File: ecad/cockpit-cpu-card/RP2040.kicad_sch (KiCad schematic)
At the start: 66 parts, among them J6 CONSOLE, J7 USB_B_Micro, J8 GamePort, SW1 USB_PGM, SW2 USB_PGM, U4 IS25LP128F-JBLE, U5 RP2040, Y1 12MHz

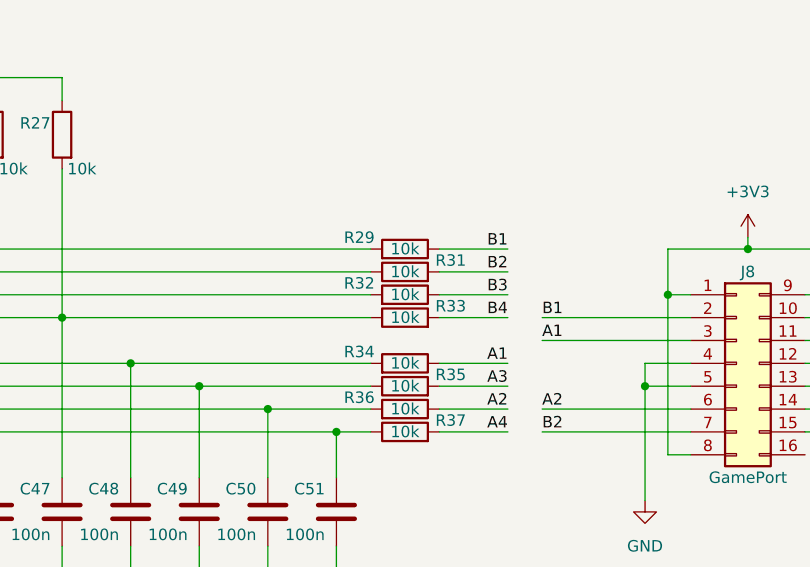
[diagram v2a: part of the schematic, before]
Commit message: Updating resistor values
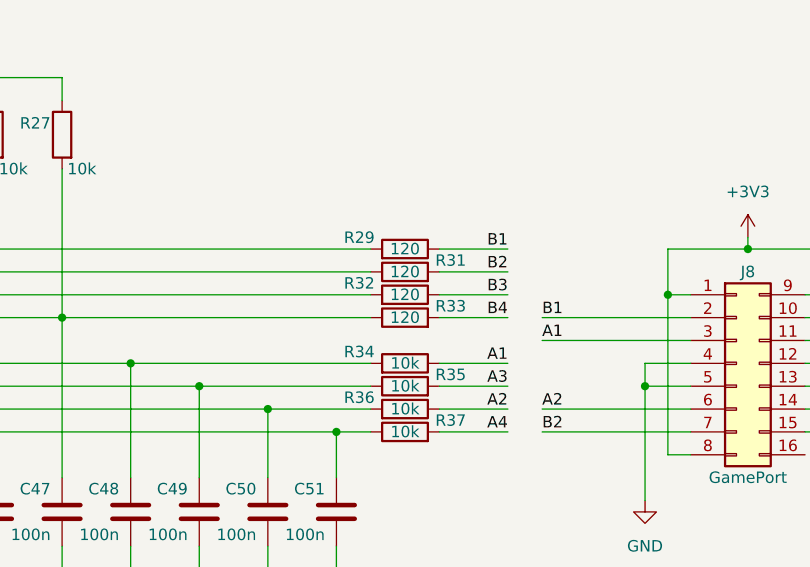
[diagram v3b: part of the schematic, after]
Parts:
- R29, R31, R32: value 10k -> 120; MPN MCMR06X103 JTL -> 1550603SAF1200T5E; ON_DISTRELEC (none) -> 300-56-474; ON_FARNELL 2073356 -> (none)
- R33: value 10k -> 120; MPN MCMR06X103 JTL -> 1550603SAF1200T5E; ON_DISTRELEC (none) -> 300-56-474
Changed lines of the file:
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@@
     (in_bom yes) (on_board yes)
     (property "Reference" "R31" (id 0) (at 218.44 118.11 90))
-    (property "Value" "10k" (id 1) (at 213.36 119.38 90))
+    (property "Value" "120" (id 1) (at 213.36 119.38 90))
     (property "Footprint" "Resistor_SMD:R_0603_1608Metric" (id 2) (at 213.36 121.158 90)
       (effects (font (size 1.27 1.27)) hide)
@@
       (effects (font (size 1.27 1.27)) hide)
     )
-    (property "MPN" "MCMR06X103 JTL" (id 4) (at 213.36 119.38 0)
-      (effects (font (size 1.27 1.27)) hide)
-    )
-    (property "ON_FARNELL" "2073356" (id 5) (at 213.36 119.38 0)
+    (property "MPN" "1550603SAF1200T5E" (id 4) (at 213.36 119.38 0)
+      (effects (font (size 1.27 1.27)) hide)
+    )
+    (property "ON_FARNELL" "" (id 5) (at 213.36 119.38 0)
+      (effects (font (size 1.27 1.27)) hide)
+    )
+    (property "ON_DISTRELEC" "300-56-474" (id 6) (at 213.36 119.38 0)
       (effects (font (size 1.27 1.27)) hide)
     )
@@
     (in_bom yes) (on_board yes)
     (property "Reference" "R29" (id 0) (at 208.28 115.57 90))
-    (property "Value" "10k" (id 1) (at 213.36 116.84 90))
+    (property "Value" "120" (id 1) (at 213.36 116.84 90))
     (property "Footprint" "Resistor_SMD:R_0603_1608Metric" (id 2) (at 213.36 118.618 90)
       (effects (font (size 1.27 1.27)) hide)
@@
       (effects (font (size 1.27 1.27)) hide)
     )
-    (property "MPN" "MCMR06X103 JTL" (id 4) (at 213.36 116.84 0)
-      (effects (font (size 1.27 1.27)) hide)
-    )
-    (property "ON_FARNELL" "2073356" (id 5) (at 213.36 116.84 0)
+    (property "MPN" "1550603SAF1200T5E" (id 4) (at 213.36 116.84 0)
+      (effects (font (size 1.27 1.27)) hide)
+    )
+    (property "ON_FARNELL" "" (id 5) (at 213.36 116.84 0)
+      (effects (font (size 1.27 1.27)) hide)
+    )
+    (property "ON_DISTRELEC" "300-56-474" (id 6) (at 213.36 116.84 0)
       (effects (font (size 1.27 1.27)) hide)
     )
@@
     (in_bom yes) (on_board yes)
     (property "Reference" "R32" (id 0) (at 208.28 120.65 90))
-    (property "Value" "10k" (id 1) (at 213.36 121.92 90))
+    (property "Value" "120" (id 1) (at 213.36 121.92 90))
     (property "Footprint" "Resistor_SMD:R_0603_1608Metric" (id 2) (at 213.36 123.698 90)
       (effects (font (size 1.27 1.27)) hide)
@@
       (effects (font (size 1.27 1.27)) hide)
     )
-    (property "MPN" "MCMR06X103 JTL" (id 4) (at 213.36 121.92 0)
-      (effects (font (size 1.27 1.27)) hide)
-    )
-    (property "ON_FARNELL" "2073356" (id 5) (at 213.36 121.92 0)
+    (property "MPN" "1550603SAF1200T5E" (id 4) (at 213.36 121.92 0)
+      (effects (font (size 1.27 1.27)) hide)
+    )
+    (property "ON_FARNELL" "" (id 5) (at 213.36 121.92 0)
+      (effects (font (size 1.27 1.27)) hide)
+    )
+    (property "ON_DISTRELEC" "300-56-474" (id 6) (at 213.36 121.92 0)
       (effects (font (size 1.27 1.27)) hide)
     )
@@
     (in_bom yes) (on_board yes)
     (property "Reference" "R33" (id 0) (at 218.44 123.19 90))
-    (property "Value" "10k" (id 1) (at 213.36 124.46 90))
+    (property "Value" "120" (id 1) (at 213.36 124.46 90))
     (property "Footprint" "Resistor_SMD:R_0603_1608Metric" (id 2) (at 213.36 126.238 90)
       (effects (font (size 1.27 1.27)) hide)
@@
       (effects (font (size 1.27 1.27)) hide)
     )
-    (property "MPN" "MCMR06X103 JTL" (id 4) (at 213.36 124.46 0)
+    (property "MPN" "1550603SAF1200T5E" (id 4) (at 213.36 124.46 0)
       (effects (font (size 1.27 1.27)) hide)
     )
@@
       (effects (font (size 1.27 1.27)) hide)
     )
+    (property "ON_DISTRELEC" "300-56-474" (id 6) (at 213.36 124.46 0)
+      (effects (font (size 1.27 1.27)) hide)
+    )

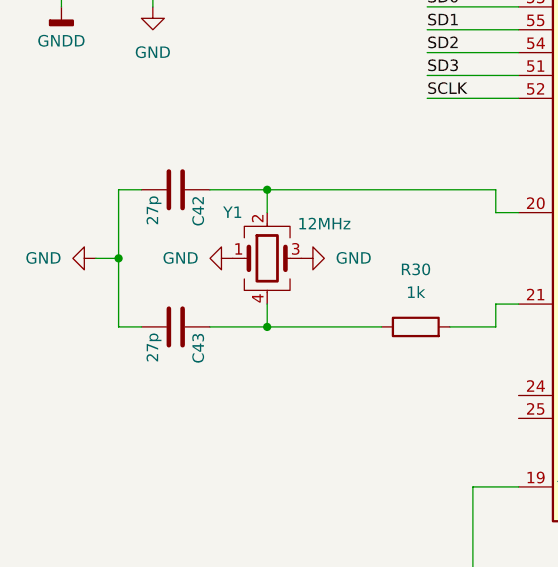
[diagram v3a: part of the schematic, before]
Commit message: Changing crystal load capacitors to 10p
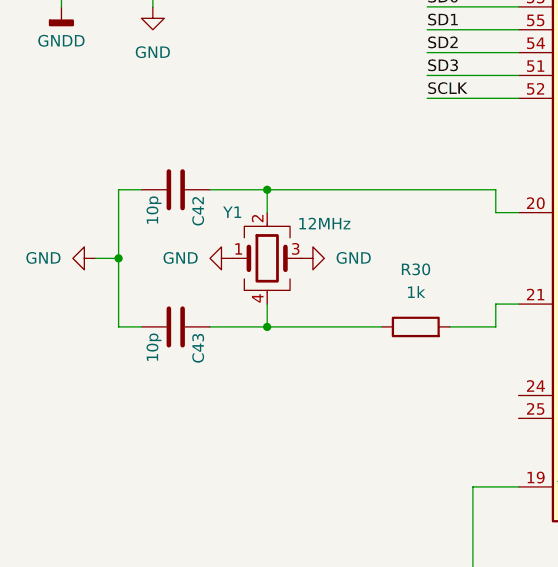
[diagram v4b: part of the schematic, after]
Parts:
- C42, C43: value 27p -> 10p; MPN C0603C270K5GACTU -> RND 1500603N100J500NT; ON_DISTRELEC (none) -> 300-86-515; ON_FARNELL 2773145 -> (none)
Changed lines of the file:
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@@
       (effects (font (size 1.27 1.27)) (justify left))
     )
-    (property "Value" "27p" (id 1) (at 30.48 104.775 0)
+    (property "Value" "10p" (id 1) (at 30.48 104.775 0)
       (effects (font (size 1.27 1.27)) (justify left))
     )
@@
       (effects (font (size 1.27 1.27)) hide)
     )
-    (property "MPN" "C0603C270K5GACTU" (id 4) (at 33.02 104.14 0)
-      (effects (font (size 1.27 1.27)) hide)
-    )
-    (property "ON_FARNELL" "2773145" (id 5) (at 33.02 104.14 0)
+    (property "MPN" "RND 1500603N100J500NT" (id 4) (at 33.02 104.14 0)
+      (effects (font (size 1.27 1.27)) hide)
+    )
+    (property "ON_FARNELL" "" (id 5) (at 33.02 104.14 0)
+      (effects (font (size 1.27 1.27)) hide)
+    )
+    (property "ON_DISTRELEC" "300-86-515" (id 6) (at 33.02 104.14 0)
       (effects (font (size 1.27 1.27)) hide)
     )
@@
       (effects (font (size 1.27 1.27)) (justify left))
     )
-    (property "Value" "27p" (id 1) (at 30.48 120.015 0)
+    (property "Value" "10p" (id 1) (at 30.48 120.015 0)
       (effects (font (size 1.27 1.27)) (justify left))
     )
@@
       (effects (font (size 1.27 1.27)) hide)
     )
-    (property "MPN" "C0603C270K5GACTU" (id 4) (at 33.02 119.38 0)
-      (effects (font (size 1.27 1.27)) hide)
-    )
-    (property "ON_FARNELL" "2773145" (id 5) (at 33.02 119.38 0)
-      (effects (font (size 1.27 1.27)) hide)
-    )
+    (property "MPN" "RND 1500603N100J500NT" (id 4) (at 33.02 119.38 0)
+      (effects (font (size 1.27 1.27)) hide)
+    )
+    (property "ON_FARNELL" "" (id 5) (at 33.02 119.38 0)
+      (effects (font (size 1.27 1.27)) hide)
+    )
+    (property "ON_DISTRELEC" "300-86-515" (id 6) (at 33.02 119.38 0)
+      (effects (font (size 1.27 1.27)) hide)
+    )
